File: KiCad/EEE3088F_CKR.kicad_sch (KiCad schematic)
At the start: 0 parts

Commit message: Significant schematic changes
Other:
- sheet Microcontroller ports: added Debugger_Potentiometer_signal, Debugger_SCL, Debugger_SDA, Debugger_Thermistor_signal, Plug_Detect; removed none
- sheet USB ports: added Debugger_Potentiometer_signal, Debugger_SCL, Debugger_SDA, Debugger_Thermistor_signal, Plug_Detect; removed none
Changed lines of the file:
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@@
     (comment 2 "This is an overview sheet showing how the sub-circuits interconnect")
   )
-  (wire (pts (xy 81.28 158.75) (xy 118.11 158.75))
+  (wire (pts (xy 81.28 107.95) (xy 118.11 107.95))
+    (stroke (width 0) (type default))
+  )
+  (wire (pts (xy 195.58 125.73) (xy 231.14 125.73))
     (stroke (width 0) (type default))
   )
@@
     (stroke (width 0) (type default))
   )
-  (wire (pts (xy 81.28 166.37) (xy 118.11 166.37))
+  (wire (pts (xy 81.28 115.57) (xy 118.11 115.57))
+    (stroke (width 0) (type default))
+  )
+  (wire (pts (xy 195.58 113.03) (xy 231.14 113.03))
     (stroke (width 0) (type default))
   )
@@
     (stroke (width 0) (type default))
   )
-  (wire (pts (xy 157.48 87.122) (xy 151.13 87.122))
-    (stroke (width 0) (type default))
-  )
-  (wire (pts (xy 160.02 90.17) (xy 160.02 57.15))
-    (stroke (width 0) (type default))
-  )
-  (wire (pts (xy 152.4 59.944) (xy 157.48 59.944))
+  (wire (pts (xy 195.58 107.95) (xy 231.14 107.95))
     (stroke (width 0) (type default))
   )
@@
     (stroke (width 0) (type default))
   )
-  (wire (pts (xy 160.02 57.15) (xy 152.4 57.15))
+  (wire (pts (xy 195.58 135.89) (xy 231.14 135.89))
     (stroke (width 0) (type default))
   )
-  (wire (pts (xy 157.48 59.944) (xy 157.48 87.122))
+  (wire (pts (xy 81.28 111.76) (xy 118.11 111.76))
     (stroke (width 0) (type default))
   )
-  (wire (pts (xy 81.28 162.56) (xy 118.11 162.56))
-    (stroke (width 0) (type default))
-  )
-  (wire (pts (xy 151.13 90.17) (xy 160.02 90.17))
+  (wire (pts (xy 195.58 121.92) (xy 231.14 121.92))
     (stroke (width 0) (type default))
   )
@@
     (stroke (width 0) (type default))
   )
-  (sheet (at 118.11 27.94) (size 34.29 38.1) (fields_autoplaced)
+  (wire (pts (xy 195.58 116.84) (xy 231.14 116.84))
+    (stroke (width 0) (type default))
+  )
+  (wire (pts (xy 195.58 132.08) (xy 231.14 132.08))
+    (stroke (width 0) (type default))
+  )
+  (sheet (at 231.14 99.06) (size 34.29 54.61) (fields_autoplaced)
     (stroke (width 0.1524) (type solid))
     (fill (color 0 0 0 0.0000))
-    (property "Sheetname" "USB" (at 118.11 27.2284 0)
+    (property "Sheetname" "USB" (at 231.14 98.3484 0)
       (effects (font (size 1.27 1.27)) (justify left bottom))
     )
-    (property "Sheetfile" "USB.kicad_sch" (at 118.11 66.6246 0)
+    (property "Sheetfile" "USB.kicad_sch" (at 231.14 154.2546 0)
       (effects (font (size 1.27 1.27)) (justify left top))
     )
-    (pin "Tx" output (at 152.4 57.15 0)
-      (effects (font (size 1.27 1.27)) (justify right))
+    (pin "Plug_Detect" output (at 231.14 107.95 180)
+      (effects (font (size 1.27 1.27)) (justify left))
     )
-    (pin "Rx" input (at 152.4 59.944 0)
-      (effects (font (size 1.27 1.27)) (justify right))
+    (pin "Rx" input (at 231.14 113.03 180)
+      (effects (font (size 1.27 1.27)) (justify left))
+    )
+    (pin "Tx" output (at 231.14 116.84 180)
+      (effects (font (size 1.27 1.27)) (justify left))
+    )
+    (pin "Debugger_Thermistor_signal" input (at 231.14 135.89 180)
+      (effects (font (size 1.27 1.27)) (justify left))
+    )
+    (pin "Debugger_Potentiometer_signal" input (at 231.14 132.08 180)
+      (effects (font (size 1.27 1.27)) (justify left))
+    )
+    (pin "Debugger_SDA" bidirectional (at 231.14 125.73 180)
+      (effects (font (size 1.27 1.27)) (justify left))
+    )
+    (pin "Debugger_SCL" bidirectional (at 231.14 121.92 180)
+      (effects (font (size 1.27 1.27)) (justify left))
     )
     (instances
@@
     )
   )
-  (sheet (at 118.11 78.74) (size 33.02 95.25) (fields_autoplaced)
+  (sheet (at 118.11 99.06) (size 77.47 54.61) (fields_autoplaced)
     (stroke (width 0.1524) (type solid))
     (fill (color 0 0 0 0.0000))
-    (property "Sheetname" "Microcontroller" (at 118.11 78.0284 0)
+    (property "Sheetname" "Microcontroller" (at 118.11 98.3484 0)
       (effects (font (size 1.27 1.27)) (justify left bottom))
     )
-    (property "Sheetfile" "microcontroller.kicad_sch" (at 118.11 174.5746 0)
+    (property "Sheetfile" "microcontroller.kicad_sch" (at 118.11 154.2546 0)
       (effects (font (size 1.27 1.27)) (justify left top))
     )
-    (pin "Sensors_SCL" output (at 118.11 158.75 180)
+    (pin "Sensors_SCL" output (at 118.11 107.95 180)
       (effects (font (size 1.27 1.27)) (justify left))
     )
-    (pin "Sensors_SDA" bidirectional (at 118.11 162.56 180)
+    (pin "Sensors_SDA" bidirectional (at 118.11 111.76 180)
       (effects (font (size 1.27 1.27)) (justify left))
     )
-    (pin "Light_interrupt" bidirectional (at 118.11 166.37 180)
+    (pin "Light_interrupt" bidirectional (at 118.11 115.57 180)
       (effects (font (size 1.27 1.27)) (justify left))
-    )
-    (pin "Rx" input (at 151.13 90.17 0)
-      (effects (font (size 1.27 1.27)) (justify right))
-    )
-    (pin "Tx" output (at 151.13 87.122 0)
-      (effects (font (size 1.27 1.27)) (justify right))
     )
     (pin "Thermistor_signal" input (at 118.11 140.97 180)
@@
       (effects (font (size 1.27 1.27)) (justify left))
     )
+    (pin "Plug_Detect" input (at 195.58 107.95 0)
+      (effects (font (size 1.27 1.27)) (justify right))
+    )
+    (pin "Rx" input (at 195.58 113.03 0)
+      (effects (font (size 1.27 1.27)) (justify right))
+    )
+    (pin "Tx" output (at 195.58 116.84 0)
+      (effects (font (size 1.27 1.27)) (justify right))
+    )
+    (pin "Debugger_SCL" bidirectional (at 195.58 121.92 0)
+      (effects (font (size 1.27 1.27)) (justify right))
+    )
+    (pin "Debugger_Potentiometer_signal" output (at 195.58 132.08 0)
+      (effects (font (size 1.27 1.27)) (justify right))
+    )
+    (pin "Debugger_Thermistor_signal" output (at 195.58 135.89 0)
+      (effects (font (size 1.27 1.27)) (justify right))
+    )
+    (pin "Debugger_SDA" bidirectional (at 195.58 125.73 0)
+      (effects (font (size 1.27 1.27)) (justify right))
+    )
     (instances
       (project "EEE3088F_CKR"
@@
     )
   )
-  (sheet (at 30.48 26.67) (size 48.26 45.72) (fields_autoplaced)
+  (sheet (at 124.46 29.21) (size 48.26 45.72) (fields_autoplaced)
     (stroke (width 0.1524) (type solid))
     (fill (color 0 0 0 0.0000))
-    (property "Sheetname" "Power" (at 30.48 25.9584 0)
+    (property "Sheetname" "Power" (at 124.46 28.4984 0)
       (effects (font (size 1.27 1.27)) (justify left bottom))
     )
-    (property "Sheetfile" "power.kicad_sch" (at 30.48 72.9746 0)
+    (property "Sheetfile" "power.kicad_sch" (at 124.46 75.5146 0)
       (effects (font (size 1.27 1.27)) (justify left top))
     )
@@
     )
   )
-  (sheet (at 31.75 100.33) (size 49.53 73.66) (fields_autoplaced)
+  (sheet (at 31.75 100.33) (size 49.53 53.34) (fields_autoplaced)
     (stroke (width 0.1524) (type solid))
     (fill (color 0 0 0 0.0000))
@@
       (effects (font (size 1.27 1.27)) (justify left bottom))
     )
-    (property "Sheetfile" "sensors.kicad_sch" (at 31.75 174.5746 0)
+    (property "Sheetfile" "sensors.kicad_sch" (at 31.75 154.2546 0)
       (effects (font (size 1.27 1.27)) (justify left top))
     )
-    (pin "Light_interrupt" bidirectional (at 81.28 166.37 0)
+    (pin "Light_interrupt" bidirectional (at 81.28 115.57 0)
       (effects (font (size 1.27 1.27)) (justify right))
     )
-    (pin "Sensors_SDA" bidirectional (at 81.28 162.56 0)
+    (pin "Sensors_SDA" bidirectional (at 81.28 111.76 0)
       (effects (font (size 1.27 1.27)) (justify right))
     )
@@
       (effects (font (size 1.27 1.27)) (justify right))
     )
-    (pin "Sensors_SCL" input (at 81.28 158.75 0)
+    (pin "Sensors_SCL" input (at 81.28 107.95 0)
       (effects (font (size 1.27 1.27)) (justify right))
     )

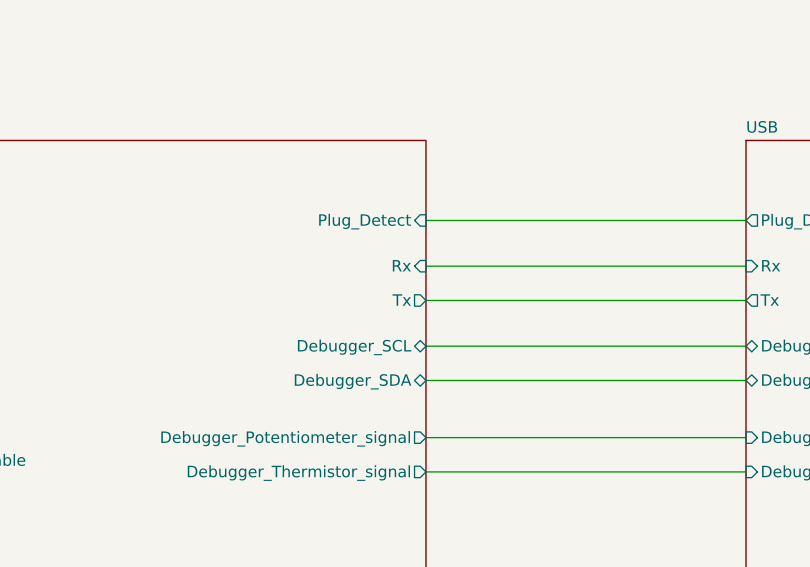
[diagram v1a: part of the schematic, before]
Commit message: Corrected all part numbers and small schematic changes
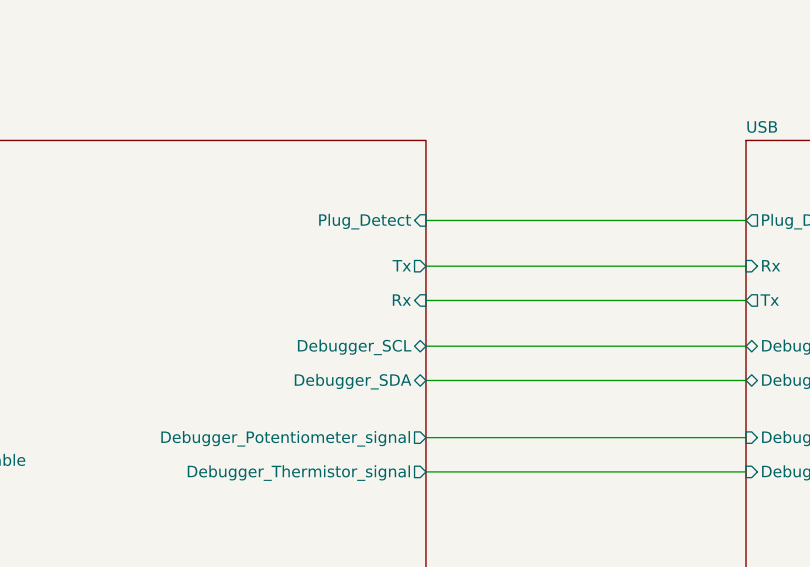
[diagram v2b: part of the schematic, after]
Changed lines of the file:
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@@
-    (stroke (width 0) (type default))
-  )
-  (wire (pts (xy 195.58 113.03) (xy 231.14 113.03))
     (stroke (width 0) (type default))
   )
@@
     (stroke (width 0) (type default))
   )
+  (wire (pts (xy 195.58 113.03) (xy 231.14 113.03))
+    (stroke (width 0) (type default))
+  )
   (wire (pts (xy 195.58 135.89) (xy 231.14 135.89))
     (stroke (width 0) (type default))
@@
     (stroke (width 0) (type default))
   )
-  (wire (pts (xy 195.58 116.84) (xy 231.14 116.84))
+  (wire (pts (xy 195.58 132.08) (xy 231.14 132.08))
     (stroke (width 0) (type default))
   )
-  (wire (pts (xy 195.58 132.08) (xy 231.14 132.08))
+  (wire (pts (xy 195.58 116.84) (xy 231.14 116.84))
     (stroke (width 0) (type default))
   )
@@
       (effects (font (size 1.27 1.27)) (justify right))
     )
-    (pin "Rx" input (at 195.58 113.03 0)
+    (pin "Rx" input (at 195.58 116.84 0)
       (effects (font (size 1.27 1.27)) (justify right))
     )
-    (pin "Tx" output (at 195.58 116.84 0)
+    (pin "Tx" output (at 195.58 113.03 0)
       (effects (font (size 1.27 1.27)) (justify right))
     )

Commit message: Lots of PCB design
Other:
- sheet Power ports: added Plug_Detect_5V; removed none
- sheet USB ports: added Plug_Detect_5V; removed none
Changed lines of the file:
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@@
+    (stroke (width 0) (type default))
+  )
+  (wire (pts (xy 250.19 99.06) (xy 250.19 60.96))
     (stroke (width 0) (type default))
   )
@@
   )
   (wire (pts (xy 195.58 107.95) (xy 231.14 107.95))
+    (stroke (width 0) (type default))
+  )
+  (wire (pts (xy 250.19 60.96) (xy 172.72 60.96))
     (stroke (width 0) (type default))
   )
@@
     (pin "Debugger_SCL" bidirectional (at 231.14 121.92 180)
       (effects (font (size 1.27 1.27)) (justify left))
+    )
+    (pin "Plug_Detect_5V" input (at 250.19 99.06 90)
+      (effects (font (size 1.27 1.27)) (justify right))
     )
     (instances
@@
       (effects (font (size 1.27 1.27)) (justify left top))
     )
+    (pin "Plug_Detect_5V" output (at 172.72 60.96 0)
+      (effects (font (size 1.27 1.27)) (justify right))
+    )
     (instances
